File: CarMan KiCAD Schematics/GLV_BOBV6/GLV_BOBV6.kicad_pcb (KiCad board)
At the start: 2 copper layers, 24 parts, among them J1 Conn_01x02, J2 Conn_01x02, J3 Conn_01x02, J4 Conn_01x02, J5 Conn_02x02_Odd_Even, J6 Conn_02x02_Odd_Even, J8 J8, J9 Conn_01x02, U1 INA226AIDGSR

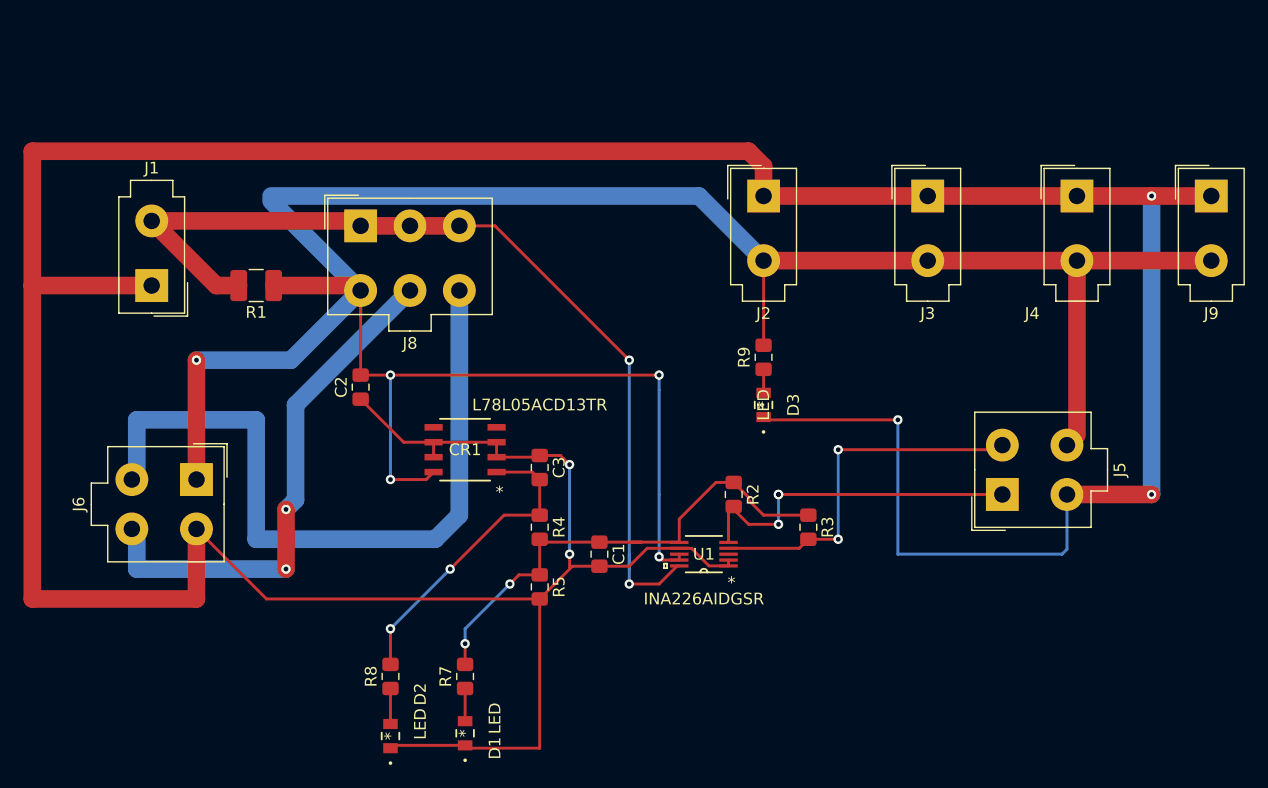
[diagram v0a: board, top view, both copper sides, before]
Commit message: GLV PCB redone to be cleaner
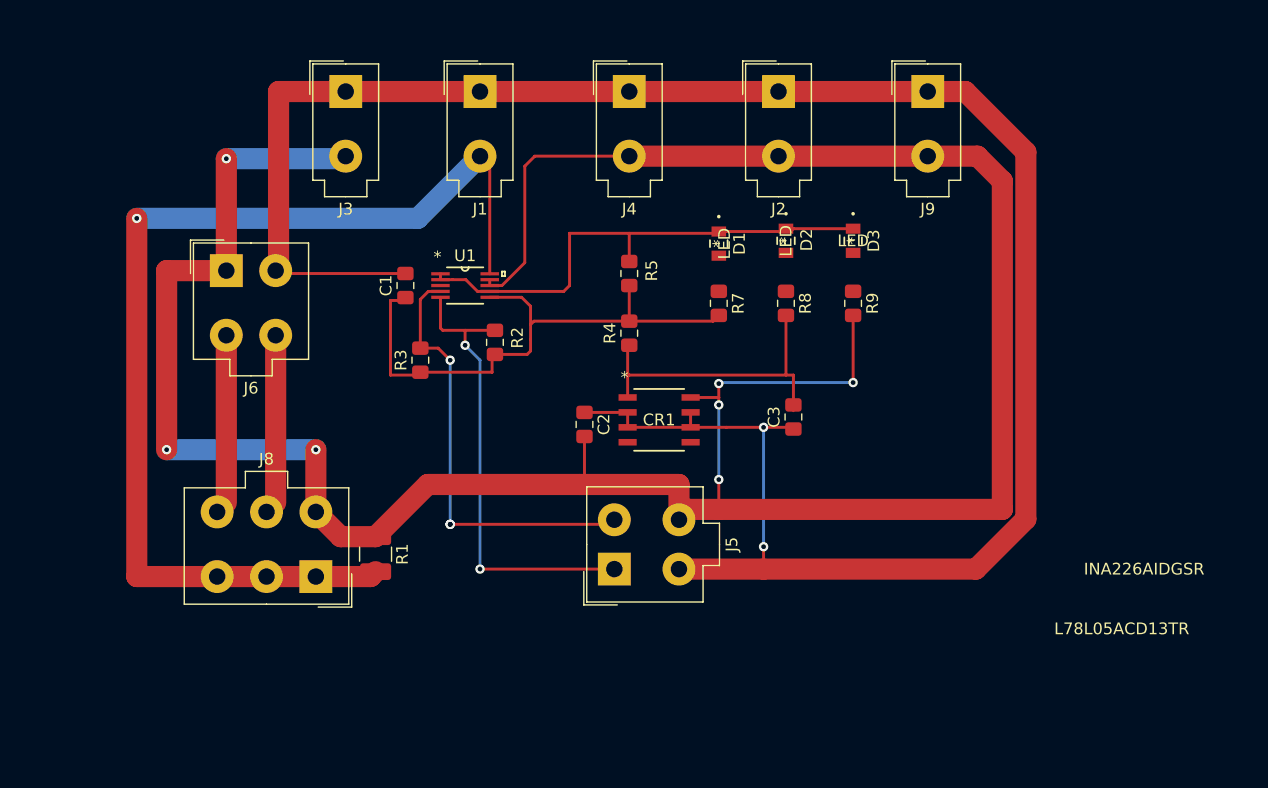
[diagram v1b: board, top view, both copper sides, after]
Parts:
- moved D2 53.9 mm to (179.7, 34.3), turned to 270 degrees
- moved J3 50.3 mm to (142.2, 21.6)
- moved D1 46.9 mm to (174.0, 34.5), turned to 270 degrees
- moved R8 46.3 mm to (179.7, 39.6), turned to 270 degrees
- moved J4 39.1 mm to (166.4, 21.6)
- moved R7 38.4 mm to (174.0, 39.6), turned to 270 degrees
- moved R3 35.9 mm to (148.6, 44.5), turned to 90 degrees
- moved J5 33.6 mm to (165.1, 62.2)
- moved J1 32.5 mm to (153.7, 21.6), turned to 0 degrees
- moved U1 30.6 mm to (152.4, 38.1), turned to 0 degrees
- moved J8 30.1 mm to (139.7, 62.9), turned to 180 degrees
- moved C1 28.2 mm to (147.3, 38.1), turned to 90 degrees
- moved R5 27.7 mm to (166.4, 37.1), turned to 90 degrees
- moved J9 25.7 mm to (191.8, 21.6)
- moved R1 25.0 mm to (144.8, 61.0), turned to 270 degrees
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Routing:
- net /GLV_RTN: track 353.7 -> 230.4 mm, vias 5 -> 2
- net /BREAKER_OUT_SL: track 62.8 -> 15.4 mm
- net /BREAKER_OUT_COOL: track 44.4 -> 15.4 mm, vias 2 -> 0
- net /24V: track 216.2 -> 239.9 mm, vias 5 -> 7
- net /BATT+: track 80.4 -> 92.7 mm, vias 2 -> 1
- net /SCL_NOT_ISO: track 29.6 -> 39.6 mm, vias 3 -> 2
- net /SDA_NOT_ISO: track 31.4 -> 37.0 mm, vias 2 -> 3
- net /3.3V_NOT_ISO: track 42.9 -> 48.4 mm, vias 2 -> 0
- net Net-(D2-Pad2): track 3.02 -> 0.00 mm
- net Net-(D1-Pad2): track 2.78 -> 0.00 mm
- net Net-(D3-Pad2): track 2.00 -> 0.00 mm
- net /5V_NOT_ISO: track 26.7 -> 26.8 mm, vias 2 -> 0

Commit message: GLV PCB edge cuts, logos, increased BATT+ trace widths, Gerber files
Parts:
- added G***: LOGO, CarMan General Footprints:Laf_College_Logo, F.Cu at (153.0, 68.6)
- added H1: MountingHole, MountingHole:MountingHole_2.5mm_Pad, F.Cu at (123.8, 22.2)
- added H2: MountingHole, MountingHole:MountingHole_2.5mm_Pad, F.Cu at (123.8, 69.8)
- added H3: MountingHole, MountingHole:MountingHole_2.5mm_Pad, F.Cu at (206.4, 22.2)
- added H4: MountingHole, MountingHole:MountingHole_2.5mm_Pad, F.Cu at (206.4, 69.8)
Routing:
- net Net-(D3-Pad2): track 0.00 -> 3.27 mm
- net Net-(D2-Pad2): track 0.00 -> 3.27 mm
- net Net-(D1-Pad2): track 0.00 -> 3.03 mm
- net /GLV_RTN: track 230.4 -> 233.4 mm
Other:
- board outline added: 95.2 x 60.3 mm
- board text added: "Electrical and Computer Engineering"
- board text added: "GLV BOB V6 Troy Coleman and Zachary Martin 11/22/20"
- board text added: "Left Side"
- board text added: "Right Side"

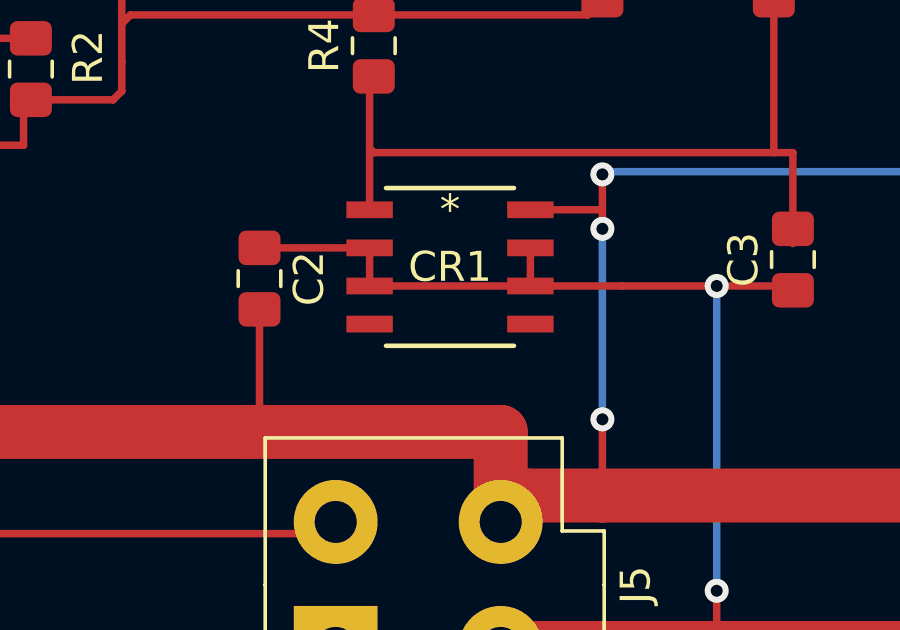
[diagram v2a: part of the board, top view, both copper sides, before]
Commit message: Logic PCB updates, Fixed I2C and ground connections in Logic
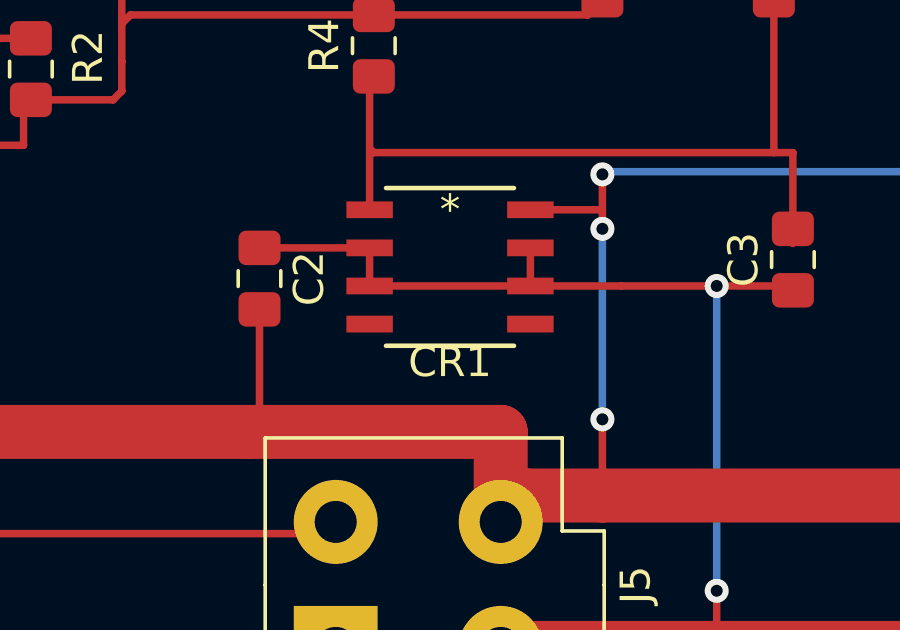
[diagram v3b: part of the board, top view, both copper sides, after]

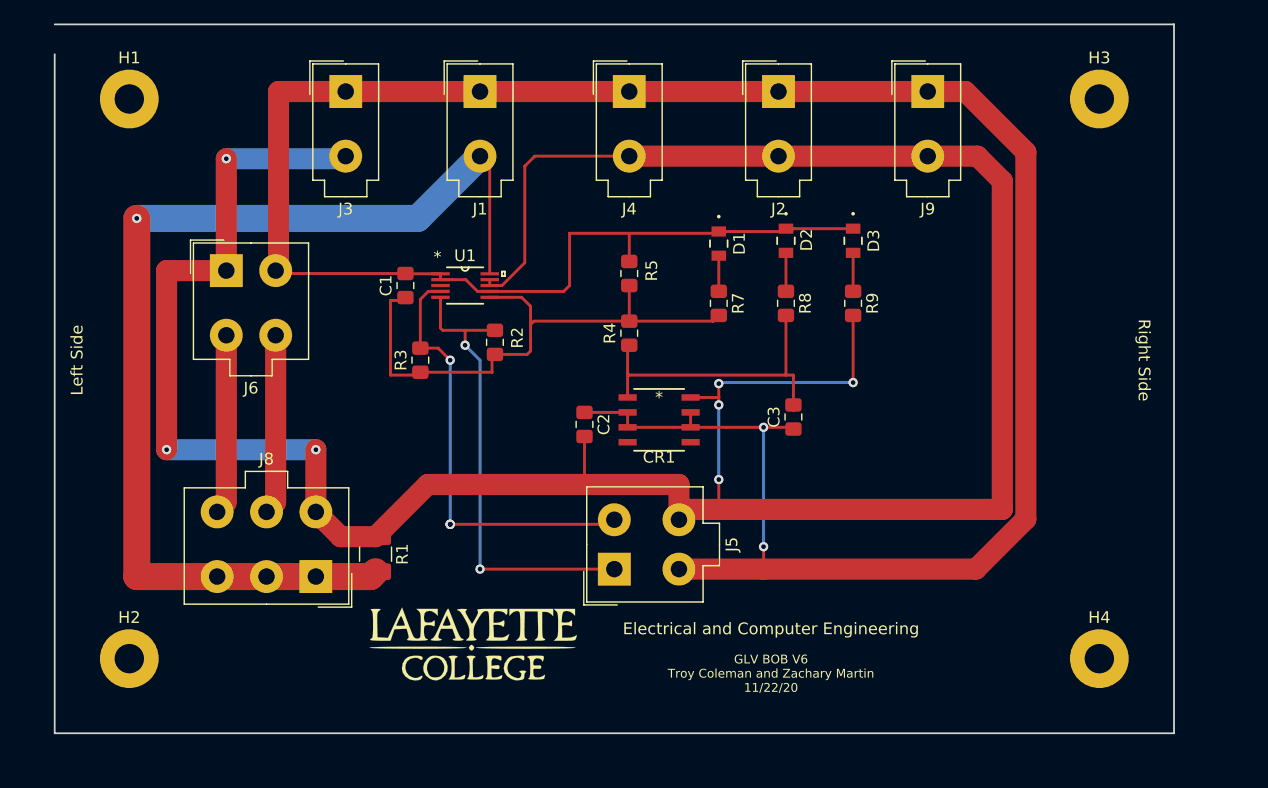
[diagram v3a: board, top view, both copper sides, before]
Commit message: GLV removed 24V to dash and 24V to BP headers. Logic almost done pending, design review
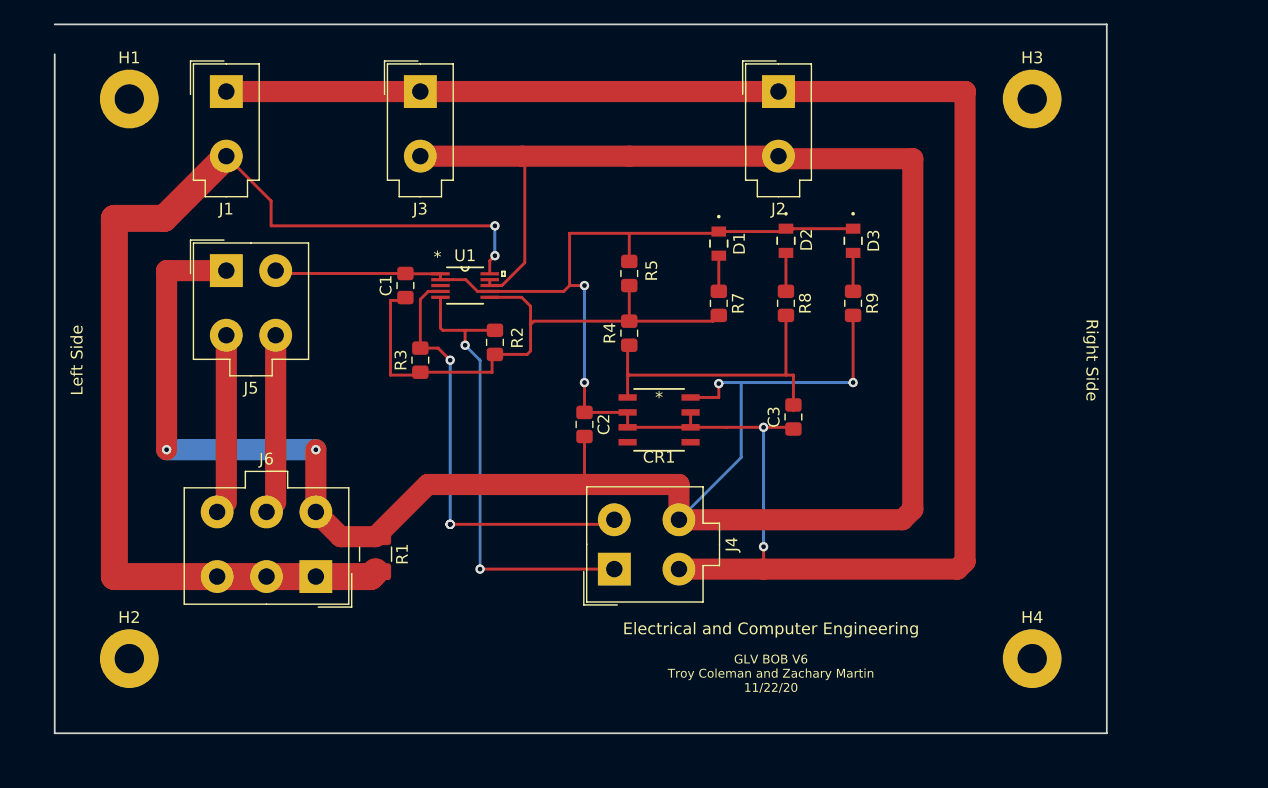
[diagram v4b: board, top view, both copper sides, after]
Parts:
- removed G***: LOGO, CarMan General Footprints:Laf_College_Logo
- removed the J4 at (166.4, 21.6)
- removed J9: Conn_01x02, CarMan General Footprints:Molex_MiniFit-JR-5556-02A_2x01x4.20mm_Straight
- J6: renamed from J8; value J8 -> J6
- moved J1 21.6 mm to (132.1, 21.6)
- moved J3 6.35 mm to (148.6, 21.6)
- moved H3 5.72 mm to (200.7, 22.2)
- moved H4 5.72 mm to (200.7, 69.8)
- renumbered J5 to J4, J6 to J5
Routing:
- net /24V: track 239.9 -> 219.9 mm, vias 7 -> 4
- net /GLV_RTN: track 233.4 -> 229.7 mm, vias 2 -> 4
- net /BATT+: track 92.7 -> 95.4 mm, vias 1 -> 2
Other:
- board size 95.2 x 60.3 mm -> 89.5 x 60.3 mm

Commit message: GLV Design Review Fixes
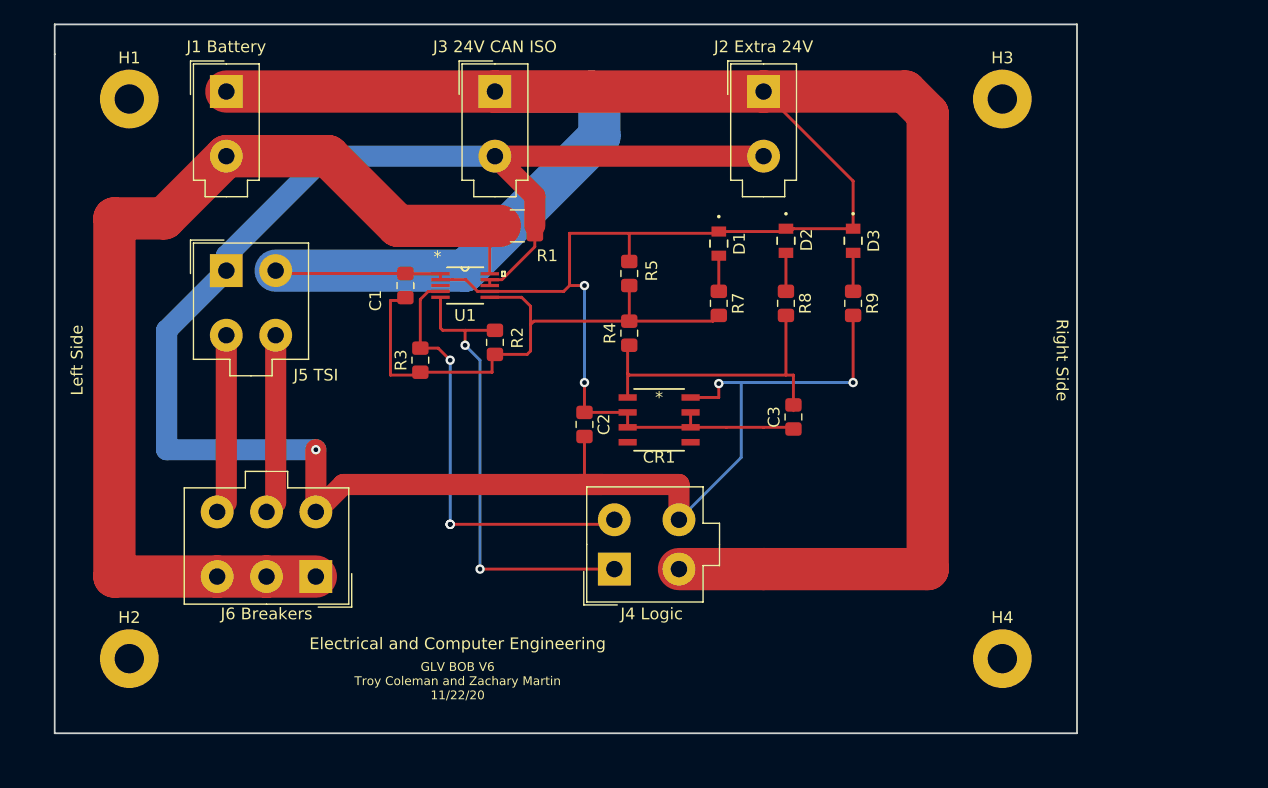
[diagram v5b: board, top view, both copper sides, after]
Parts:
- J1 Battery: renamed from J1
- J2 Extra 24V: renamed from J2
- J3 24V CAN ISO: renamed from J3
- J4 Logic: renamed from J4
- J5 TSI: renamed from J5
- J6 Breakers: renamed from J6
- moved R1 30.4 mm to (156.8, 33.0), turned to 180 degrees
- moved J3 24V CAN ISO 6.35 mm to (154.9, 21.6)
- moved H3 2.54 mm to (198.1, 22.2)
- moved H4 2.54 mm to (198.1, 69.8)
- moved J2 Extra 24V 1.27 mm to (177.8, 21.6)
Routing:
- net /24V: track 219.9 -> 176.6 mm, vias 4 -> 3
- net /GLV_RTN: track 229.7 -> 270.0 mm, vias 4 -> 2
- net /BATT+: track 95.4 -> 89.5 mm, vias 2 -> 0
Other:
- board size 89.5 x 60.3 mm -> 87 x 60.3 mm

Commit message: Changed order of names on TSI Board
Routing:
- net /GLV_RTN: track 270.0 -> 72.2 mm
- added copper zone on B.Cu, net /GLV_RTN
